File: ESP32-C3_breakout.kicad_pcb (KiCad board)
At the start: 2 copper layers, 13 parts, among them J1 Conn_01x08_Male, J2 Conn_01x08_Male, U2 ESP32-C3, Y1 40MHz

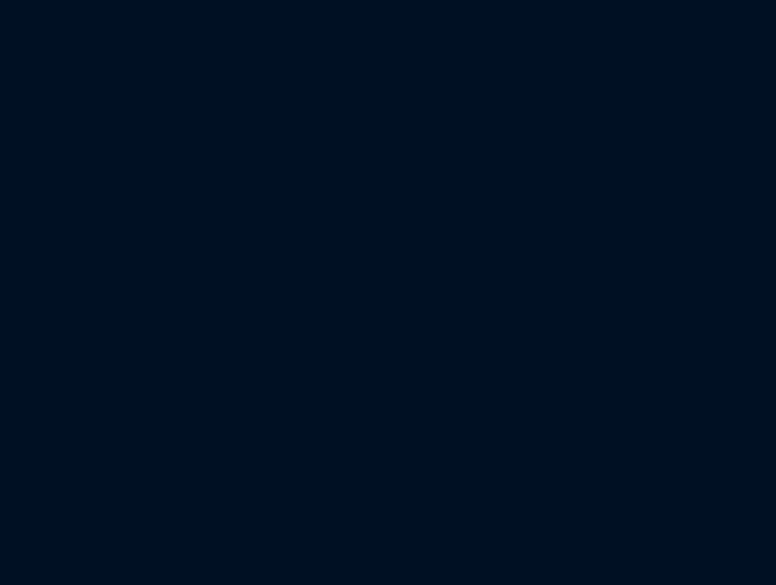
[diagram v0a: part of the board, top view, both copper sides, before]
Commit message: Added LDO
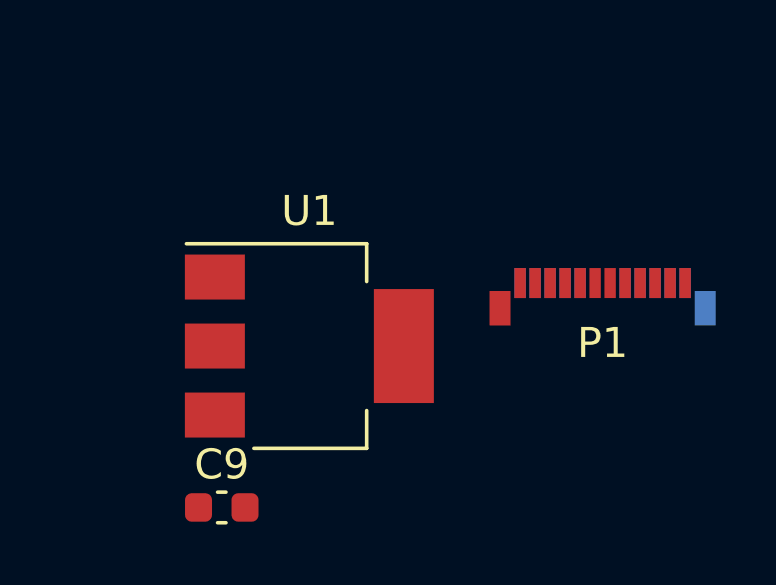
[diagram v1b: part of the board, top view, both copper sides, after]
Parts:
- added C9: 0.1u, Capacitor_SMD:C_0603_1608Metric, F.Cu at (191.0, 107.4)
- added P1: USB_C_Plug, Connector_USB:USB_C_Plug_Molex_105444, F.Cu at (203.7, 99.9)
- added U1: LD1117S33TR_SOT223, Package_TO_SOT_SMD:SOT-223-3_TabPin2, F.Cu at (193.9, 102.1)
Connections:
- C4 pad 1: Net-(C4-Pad1) -> +3V3
- C5 pad 1: Net-(C4-Pad1) -> +3V3
- C6 pad 1: Net-(C4-Pad1) -> +3V3
- U2 pad 1: unconnected-(U2-Pad1) -> ANT
- U2 pad 11: unconnected-(U2-Pad11) -> +3V3
- U2 pad 14: unconnected-(U2-Pad14) -> Net-(U2-Pad14)
- U2 pad 17: unconnected-(U2-Pad17) -> +3V3
- U2 pad 32: unconnected-(U2-Pad32) -> +3V3
- U2 pad 6: unconnected-(U2-Pad6) -> Net-(U2-Pad6)

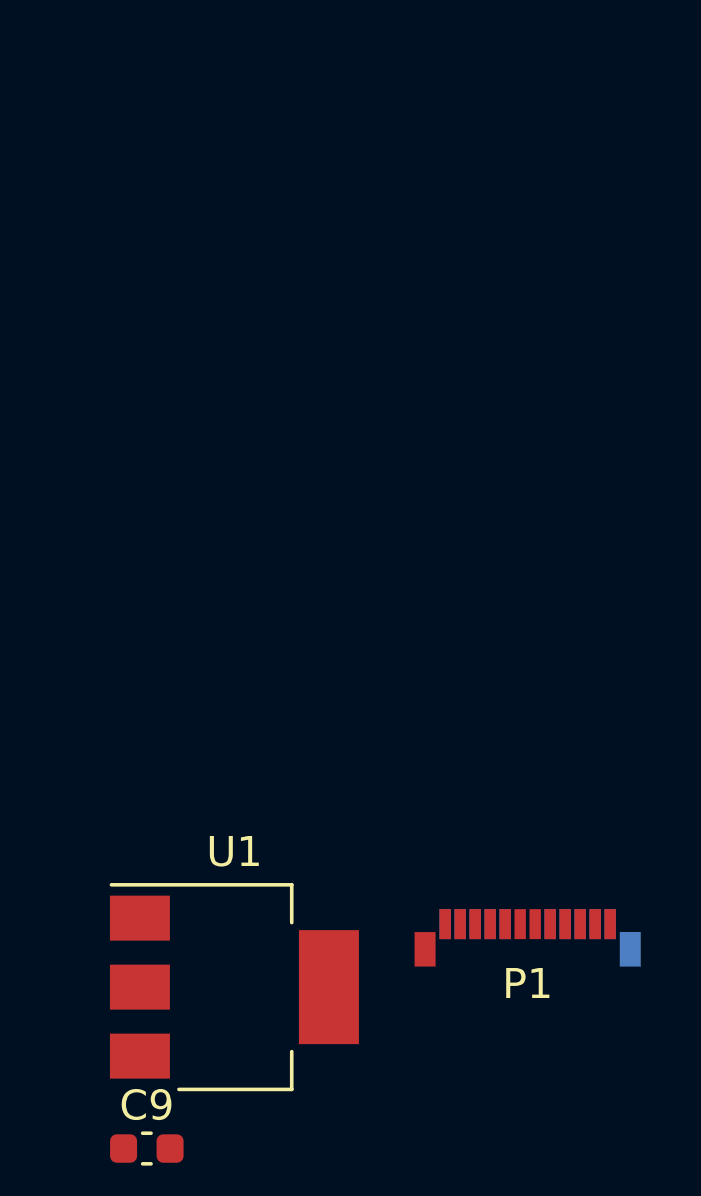
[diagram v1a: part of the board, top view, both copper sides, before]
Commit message: Added USB-C
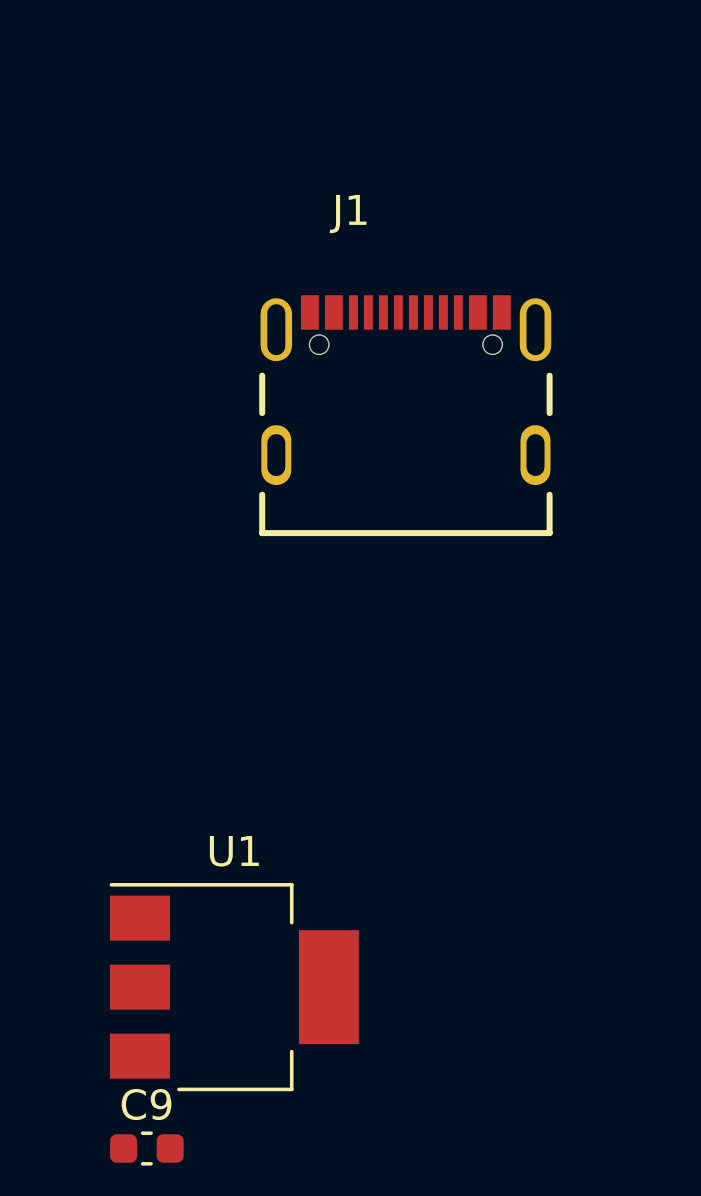
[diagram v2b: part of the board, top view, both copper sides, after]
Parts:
- removed P1: USB_C_Plug, Connector_USB:USB_C_Plug_Molex_105444
- added J1: USB4105-GF-A, USB4105-GF-A:GCT_USB4105-GF-A, F.Cu at (199.6, 84.3)

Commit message: General improvements
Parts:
- removed the J1 at (161.5, 73.7)
- removed the J1 at (199.6, 84.3)
- added C10: 10u, Capacitor_SMD:C_0603_1608Metric, F.Cu at (219.7, 122.7)
- added C11: 1u, Capacitor_SMD:C_0603_1608Metric, F.Cu at (219.7, 115.2)
- added C12: 10u, Capacitor_SMD:C_0603_1608Metric, F.Cu at (223.7, 115.2)
- added J1: USB4105-GF-A, USB4105-GF-A:GCT_USB4105-GF-A, F.Cu at (149.1, 71.6)
- added J3: Conn_01x11_Male, Connector_PinHeader_2.54mm:PinHeader_1x11_P2.54mm_Vertical, B.Cu at (159.0, 63.0)
- added R3: 10k, Resistor_SMD:R_0603_1608Metric, F.Cu at (223.7, 117.7)
- added R4: 5k1, Resistor_SMD:R_0603_1608Metric, F.Cu at (219.7, 120.2)
- added R5: 5k1, Resistor_SMD:R_0603_1608Metric, F.Cu at (219.7, 117.7)
- added SW1: SW_Push, Button_Switch_SMD:SW_SPST_FSMSM, F.Cu at (211.2, 121.5)
- added SW2: SW_Push, Button_Switch_SMD:SW_SPST_FSMSM, F.Cu at (211.2, 116.4)
- added U3: WE-TVS-82400102, Package_TO_SOT_SMD:SOT-23-6, F.Cu at (158.2, 76.2)
- J2: value Conn_01x08_Male -> Conn_01x11_Male; footprint Connector_PinHeader_2.54mm:PinHeader_1x08_P2.54mm_Vertical -> Connector_PinHeader_2.54mm:PinHeader_1x11_P2.54mm_Vertical; moved to B.Cu
- moved U1 46.6 mm to (160.5, 69.6)
- moved U2 13.6 mm to (180.6, 71.1), turned to -135 degrees
- moved J2 7.42 mm to (159.0, 80.8), turned to -90 degrees
- moved Y1 4.66 mm to (184.4, 74.4), turned to 45 degrees
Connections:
- net Net-(C1-Pad1) renamed /EN
- J2 pad 1: unconnected-(J2-Pad1) -> /GPIO0
- J2 pad 2: unconnected-(J2-Pad2) -> /GPIO1
- J2 pad 3: unconnected-(J2-Pad3) -> /GPIO2
- J2 pad 4: unconnected-(J2-Pad4) -> /GPIO3
- J2 pad 5: unconnected-(J2-Pad5) -> /GPIO4
- J2 pad 6: unconnected-(J2-Pad6) -> /GPIO5
- J2 pad 7: unconnected-(J2-Pad7) -> /GPIO6
- J2 pad 8: unconnected-(J2-Pad8) -> /GPIO7
- U1 pad 2: unconnected-(U1-Pad2) -> +3V3
- U1 pad 3: unconnected-(U1-Pad3) -> VDD
- U2 pad 14: Net-(R2-Pad2) -> unconnected-(U2-Pad14)
- U2 pad 15: unconnected-(U2-Pad15) -> /BOOT
- U2 pad 25: unconnected-(U2-Pad25) -> /USB_D-
- U2 pad 26: unconnected-(U2-Pad26) -> /USB_D+
- U2 pad 29: Net-(U2-Pad29) -> Net-(C7-Pad1)
- U2 pad 30: Net-(U2-Pad30) -> Net-(C8-Pad1)
- Y1 pad 1: Net-(U2-Pad30) -> unconnected-(Y1-Pad1)
- Y1 pad 2: Net-(C7-Pad1) -> Net-(C8-Pad1)
- Y1 pad 3: Net-(U2-Pad29) -> unconnected-(Y1-Pad3)
- Y1 pad 4: Net-(C8-Pad1) -> Net-(C7-Pad1)
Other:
- board outline added: 49.5 x 21.3 mm

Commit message: Improved schematics
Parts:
- added R2: 10k, Resistor_SMD:R_0603_1608Metric, F.Cu at (170.2, 84.1)
- C7, C8: value 10u -> 10p
- SW1, SW2: footprint Button_Switch_SMD:SW_SPST_FSMSM -> Button_Switch_SMD:SW_SPST_PTS810
- moved C12 81.1 mm to (157.5, 68.3), turned to 90 degrees
- moved SW2 80.3 mm to (150.6, 63.8)
- moved C10 79.9 mm to (157.5, 72.6), turned to -90 degrees
- moved SW1 74.1 mm to (150.4, 79.2)
- moved R3 68.6 mm to (168.1, 77.5)
- moved C11 68.1 mm to (168.4, 70.4), turned to -90 degrees
- moved R4 65.8 mm to (163.1, 86.6), turned to 180 degrees
- moved R5 65.3 mm to (163.1, 85.1)
- moved C9 43.3 mm to (172.0, 68.6)
- moved C5 34.6 mm to (172.0, 71.9)
- moved C2 30.9 mm to (183.6, 73.7), turned to -45 degrees
- moved C6 30.5 mm to (172.2, 73.4)
- moved C4 30.2 mm to (172.0, 76.2)
- moved R1 29.1 mm to (155.4, 78.2), turned to 180 degrees
- moved J2 25.4 mm to (184.4, 80.8), turned to 90 degrees
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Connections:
- net ANT renamed /ANT
- J2 pad 1: /GPIO0 -> GND
- J2 pad 10: /GPIO9 -> VDD
- J2 pad 11: /GPIO10 -> GND
- J2 pad 2: /GPIO1 -> +3V3
- J2 pad 3: /GPIO2 -> /GPIO0
- J2 pad 4: /GPIO3 -> /GPIO1
- J2 pad 5: /GPIO4 -> /GPIO2
- J2 pad 6: /GPIO5 -> /GPIO3
- J2 pad 7: /GPIO6 -> /GPIO4
- J2 pad 8: /GPIO7 -> /GPIO5
- J2 pad 9: /GPIO8 -> /GPIO6
- J3 pad 1: /EN -> GND
- J3 pad 10: unconnected-(J3-Pad10) -> VDD
- J3 pad 11: unconnected-(J3-Pad11) -> GND
- J3 pad 2: /RX -> +3V3
- J3 pad 3: /TX -> /EN
- J3 pad 4: unconnected-(J3-Pad4) -> /RX
- J3 pad 5: unconnected-(J3-Pad5) -> /TX
- J3 pad 6: unconnected-(J3-Pad6) -> /GPIO7
- J3 pad 7: unconnected-(J3-Pad7) -> /GPIO8
- J3 pad 8: unconnected-(J3-Pad8) -> /GPIO9
- J3 pad 9: unconnected-(J3-Pad9) -> /GPIO10
- R3 pad 2: Net-(R3-Pad2) -> /GPIO8
- U2 pad 10: unconnected-(U2-Pad10) -> /GPIO5
- U2 pad 12: unconnected-(U2-Pad12) -> /GPIO6
- U2 pad 13: unconnected-(U2-Pad13) -> /GPIO7
- U2 pad 14: unconnected-(U2-Pad14) -> /GPIO8
- U2 pad 16: unconnected-(U2-Pad16) -> /GPIO10
- U2 pad 2: Net-(L1-Pad2) -> +3V3
- U2 pad 27: unconnected-(U2-Pad27) -> /RX
- U2 pad 28: unconnected-(U2-Pad28) -> /TX
- U2 pad 3: Net-(L1-Pad2) -> +3V3
- U2 pad 4: unconnected-(U2-Pad4) -> /GPIO0
- U2 pad 5: unconnected-(U2-Pad5) -> /GPIO1
- U2 pad 6: Net-(R3-Pad2) -> /GPIO2
- U2 pad 8: unconnected-(U2-Pad8) -> /GPIO3
- U2 pad 9: unconnected-(U2-Pad9) -> /GPIO4
- Y1 pad 1: unconnected-(Y1-Pad1) -> GND
- Y1 pad 3: unconnected-(Y1-Pad3) -> GND
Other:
- outline, holes or cut-outs redrawn
- board text added: "Button footprint is not final"

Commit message: Further improvements
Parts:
- removed U3: WE-TVS-82400102, Package_TO_SOT_SMD:SOT-23-6
- added AE1: Antenna, ESP_Antenna:ESPRESSIF_ESP32_MIFA_2.4GHz_Right, F.Cu at (189.9, 67.3)
- added C13: C, Capacitor_SMD:C_0603_1608Metric, F.Cu at (183.4, 70.9)
- added C14: C, Capacitor_SMD:C_0603_1608Metric, F.Cu at (187.7, 66.5)
- added D1: C4D10120D, Package_TO_SOT_SMD:SOT-223, F.Cu at (167.1, 75.4)
- added L1: L, Inductor_SMD:L_0603_1608Metric, F.Cu at (184.4, 68.6)
- added R6: 10k, Resistor_SMD:R_0603_1608Metric, F.Cu at (174.5, 76.5)
- added R7: 10k, Resistor_SMD:R_0603_1608Metric, F.Cu at (174.5, 78.0)
- moved R1 27.4 mm to (179.3, 64.8)
- moved R2 16.7 mm to (173.0, 67.6), turned to 90 degrees
- moved C3 16.6 mm to (185.7, 72.9)
- moved C6 14.6 mm to (186.7, 71.9), turned to -45 degrees
- moved C4 14.2 mm to (182.6, 66.8), turned to 45 degrees
- moved C5 11.4 mm to (181.6, 65.8), turned to 45 degrees
- moved R5 10.9 mm to (161.0, 74.4)
- moved R4 10.1 mm to (161.0, 76.7), turned to 0 degrees
- moved R3 8.18 mm to (173.0, 70.9), turned to 90 degrees
- moved C11 7.62 mm to (161.8, 66.5), turned to 90 degrees
- moved C9 5.43 mm to (173.0, 73.9), turned to -90 degrees
- moved C10 4.58 mm to (161.8, 71.1)
- moved U1 4.50 mm to (167.1, 68.3)
- moved C12 3.94 mm to (160.3, 65.5)
- moved J1 3.81 mm to (152.9, 71.9)
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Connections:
- net Net-(J1-PadA6) renamed /D_P
- net Net-(J1-PadA7) renamed /D_N
- J1 pad A4_B9: VDD -> /USB_+5V
- J1 pad B4_A9: VDD -> /USB_+5V
- J2 pad 10: VDD -> GND
- J2 pad 11: GND -> /VIN
- J2 pad 2: +3V3 -> GND
- J2 pad 3: /GPIO0 -> /TX
- J2 pad 4: /GPIO1 -> /RX
- J2 pad 5: /GPIO2 -> /GPIO10
- J2 pad 6: /GPIO3 -> /GPIO9
- J2 pad 7: /GPIO4 -> /GPIO8
- J2 pad 8: /GPIO5 -> /GPIO7
- J3 pad 10: VDD -> GND
- J3 pad 11: GND -> /USB_+5V
- J3 pad 4: /RX -> /GPIO0
- J3 pad 5: /TX -> /GPIO1
- J3 pad 6: /GPIO7 -> /GPIO2
- J3 pad 7: /GPIO8 -> /GPIO3
- J3 pad 8: /GPIO9 -> /GPIO4
- J3 pad 9: /GPIO10 -> /GPIO5
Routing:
- net +3V3: track 0.00 -> 75.0 mm, vias 0 -> 4
- net /EN: track 0.00 -> 66.3 mm, vias 0 -> 1
- net /BOOT: track 0.00 -> 31.4 mm, vias 0 -> 3
- net /D_N: track 0.00 -> 27.2 mm, vias 0 -> 3
- net /D_P: track 0.00 -> 27.0 mm, vias 0 -> 2
- net /GPIO6: track 0.00 -> 23.7 mm, vias 0 -> 1
- net /GPIO5: track 0.00 -> 21.6 mm, vias 0 -> 1
- net /USB_+5V: track 0.00 -> 20.2 mm
- net /GPIO7: track 0.00 -> 20.0 mm, vias 0 -> 1
- net /GPIO8: track 0.00 -> 17.8 mm, vias 0 -> 2
- net Net-(J1-PadA5): track 0.00 -> 17.1 mm
- net /GPIO2: track 0.00 -> 15.9 mm, vias 0 -> 2
- net /GPIO4: track 0.00 -> 15.2 mm
- net /GPIO3: track 0.00 -> 13.3 mm
- net /GPIO1: track 0.00 -> 12.5 mm, vias 0 -> 1
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- added copper zone on B.Cu, net GND
- added copper zone on F.Cu, net GND
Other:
- board size 49.5 x 21.3 mm -> 45.7 x 21.3 mm
- board text added: "2022"
- board text added: "3V3"
- board text added: "5V IN"
- board text added: "EN"
- board text added: "ESP32-C3 NANO"
- board text added: "GND"
- board text added: "GPIO0"
- board text added: "GPIO1"
- board text added: "GPIO10"
- board text added: "GPIO2"
- board text added: "GPIO3"
- board text added: "GPIO4"
- board text added: "GPIO5"
- board text added: "GPIO6"
- board text added: "GPIO7"
- board text added: "GPIO8"
- board text added: "GPIO9"
- board text added: "RX"
- board text added: "SZKANDERA & FRYCAK"
- board text added: "TX"
- board text added: "USB 5V"
- board text removed: "Button footprint is not final"
